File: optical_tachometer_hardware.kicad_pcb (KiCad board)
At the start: 2 copper layers, 0 parts

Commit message: Add all hardware to layout file
Supports #5.
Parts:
- added C1: 0.1uF, Capacitor_SMD:C_0805_2012Metric, F.Cu at (0.00, 0.00)
- added D1: TCRT5000, vishay:tcrt5000, F.Cu at (16.9, -7.14)
- added D2: GREEN, LED_SMD:LED_0805_2012Metric, F.Cu at (4.47, 0.01)
- added D3: BLUE, LED_SMD:LED_0805_2012Metric, F.Cu at (8.92, 0.01)
- added J1: J1, Connector_PinHeader_2.54mm:PinHeader_1x03_P2.54mm_Horizontal, F.Cu at (0.10, -8.88)
- added Q1: 2N2222, Package_TO_SOT_THT:TO-92_HandSolder, F.Cu at (13.2, 0.49)
- added R1: 100, Resistor_SMD:R_0603_1608Metric, F.Cu at (-0.22, 2.79)
- added R2: 10k, Resistor_SMD:R_0603_1608Metric, F.Cu at (3.79, 2.79)
- added R3: 330, Resistor_SMD:R_0603_1608Metric, F.Cu at (7.80, 2.79)
- added R4: 330, Resistor_SMD:R_0603_1608Metric, F.Cu at (19.7, -1.83)

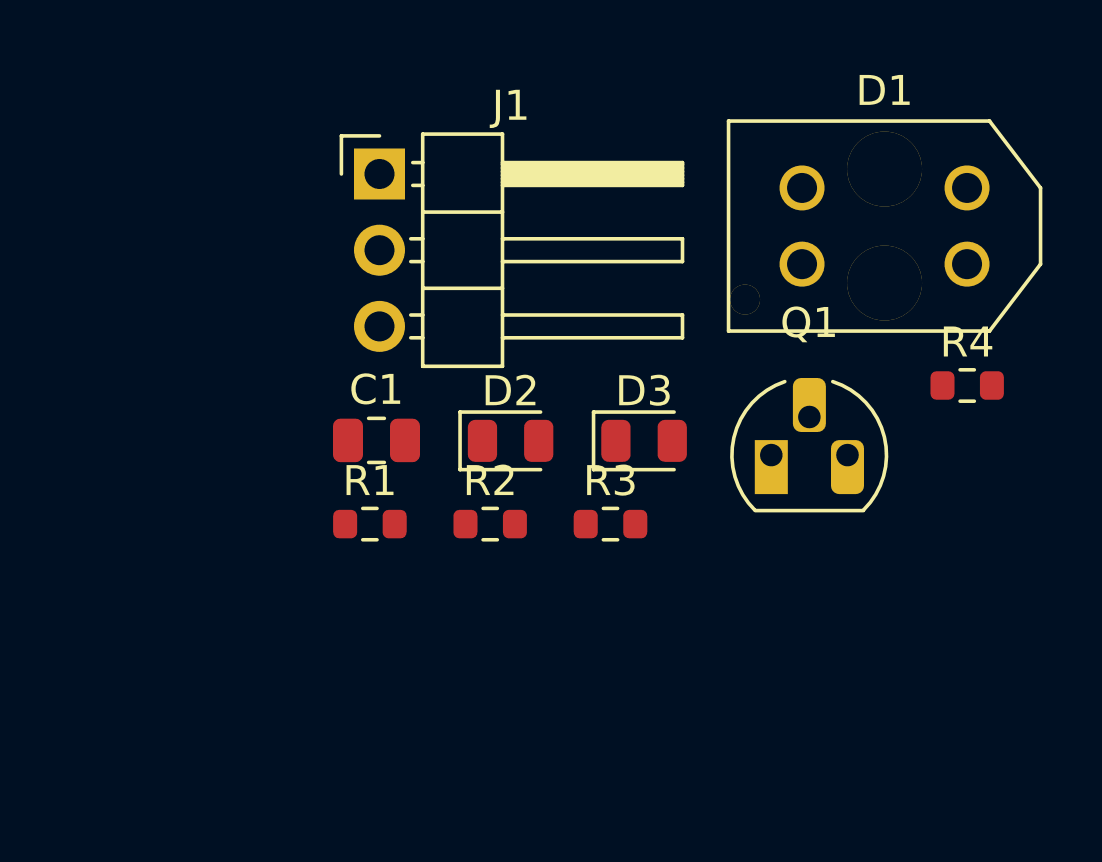
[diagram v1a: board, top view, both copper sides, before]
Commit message: Complete initial layout
Supports #5.
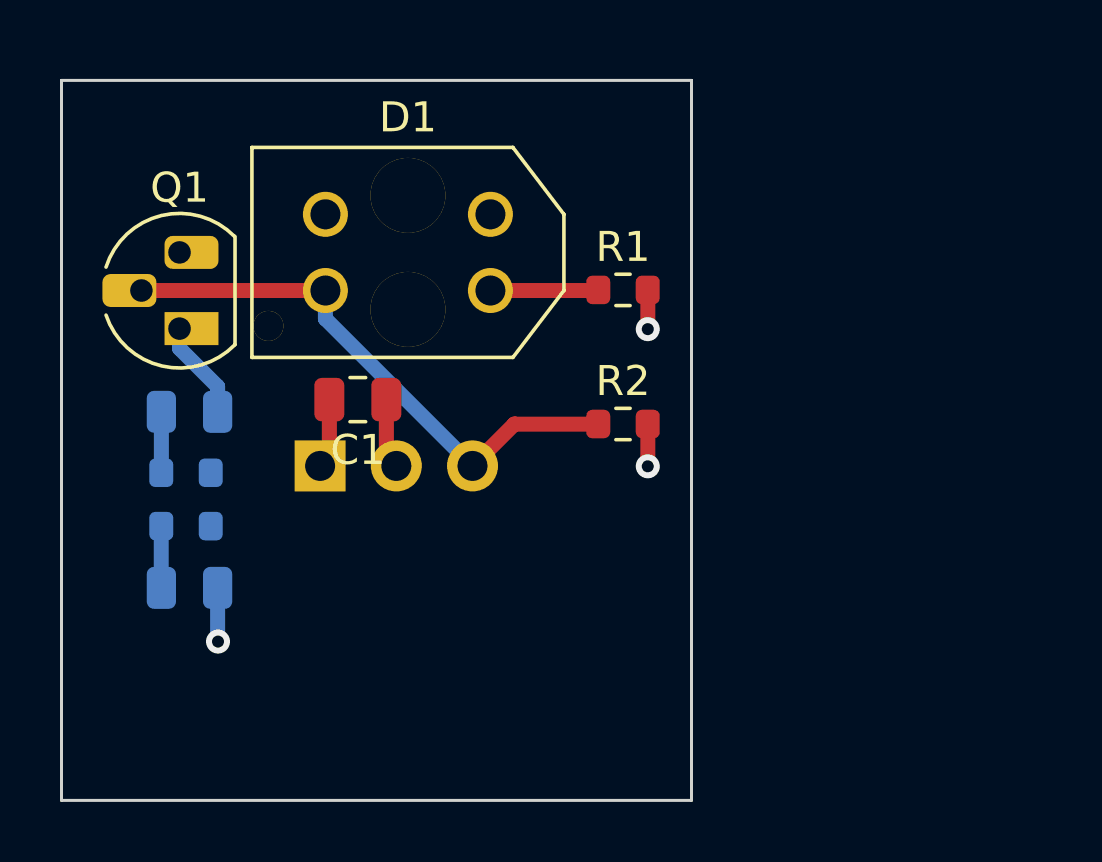
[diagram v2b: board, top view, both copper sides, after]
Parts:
- D2, D3, J1, R3, R4: moved to B.Cu
- moved R4 26.5 mm to (-6.35, 2.86)
- moved Q1 20.2 mm to (-6.57, -3.73), turned to 90 degrees
- moved D3 15.9 mm to (-6.23, 4.91)
- moved D1 15.9 mm to (1.05, -6.27)
- moved R3 14.3 mm to (-6.35, 1.08)
- moved R1 11.5 mm to (8.22, -5.02)
- moved D2 10.7 mm to (-6.23, -0.95)
- moved J1 9.93 mm to (-1.88, 0.85), turned to 270 degrees
- moved R2 5.54 mm to (8.22, -0.55)
- moved C1 1.49 mm to (-0.62, -1.36), turned to 180 degrees
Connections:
- net +5V renamed VCC
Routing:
- net SENSOR_OUTPUT: track 0.00 -> 18.8 mm
- net GND: track 0.00 -> 5.06 mm, vias 0 -> 2
- net VCC: track 0.00 -> 4.14 mm, vias 0 -> 1
- net Net-(D1-Pad4): track 0.00 -> 3.60 mm
- net Net-(D2-Pad2): track 0.00 -> 3.30 mm
- net Net-(D3-Pad1): track 0.00 -> 2.06 mm
- net Net-(D2-Pad1): track 0.00 -> 2.03 mm
- added copper zone on B.Cu, net GND
- added copper zone on F.Cu, net VCC
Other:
- board outline added: 21 x 24 mm

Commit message: Add silk (logo, number) to pcb
Supports #5.
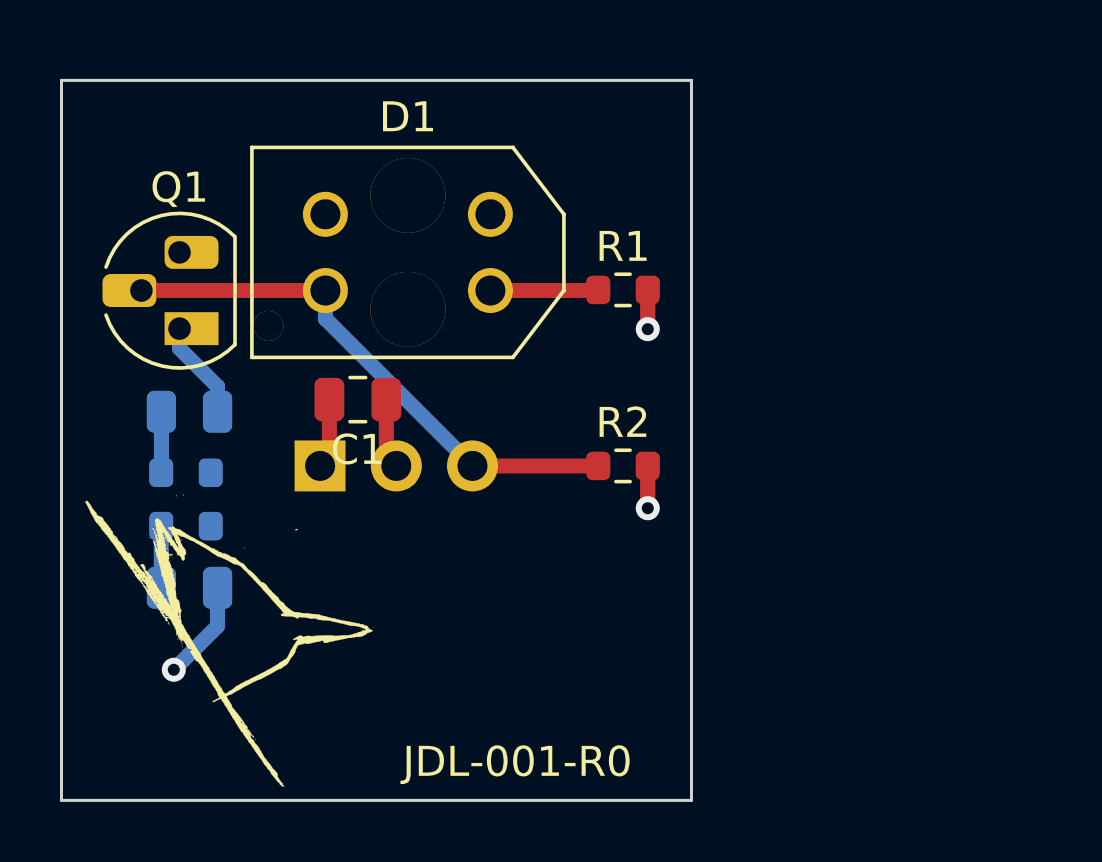
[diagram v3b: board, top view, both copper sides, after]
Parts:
- added G***: LOGO, graphics:jaybird-logo-small, F.Cu at (-4.93, 6.81)
- moved R2 1.40 mm to (8.22, 0.85)
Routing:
- net VCC: track 4.14 -> 5.68 mm
- net SENSOR_OUTPUT: track 18.8 -> 18.2 mm
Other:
- board text added: "JDL-001-R0"
